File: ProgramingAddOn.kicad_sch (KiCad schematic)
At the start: 25 parts, among them J1 USB_B_Mini, J4 Conn_01x12_Male, J5 Conn_01x12_Female, SW1 SW_DIP_x02, SW2 SW_Push, SW3 SW_Push, SW4 SW_Push, SW5 SW_DIP_x04, SW6 SW_Push, SW7 SW_DIP_x04, U1 CP2102N-Axx-xQFN20

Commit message: Add schematic PDF and PCB rendering
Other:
- company: (none) -> Eric Dynowski
- title: (none) -> SuperCon Badge Programer with USB
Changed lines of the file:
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@@
 (kicad_sch (version 20211123) (generator eeschema)
   (paper "A4")
+  (title_block
+    (title "SuperCon Badge Programer with USB")
+    (date "11/12/22")
+    (rev "v0.1")
+    (company "Eric Dynowski")
+  )
   (junction (at 181.61 67.31) (diameter 0) (color 0 0 0 0)
   )

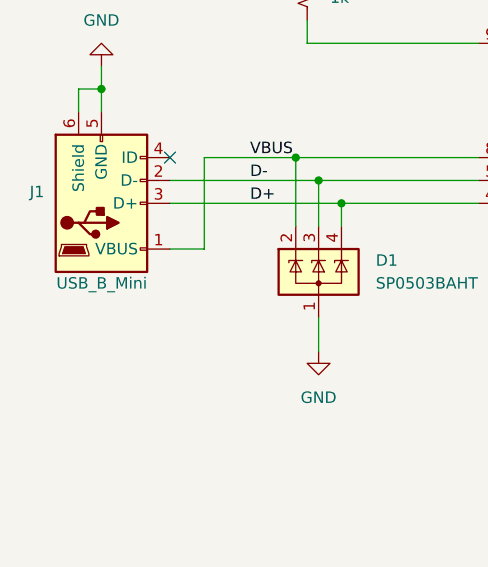
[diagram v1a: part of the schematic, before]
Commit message: Update part descriptions. Change USB mini to micro.
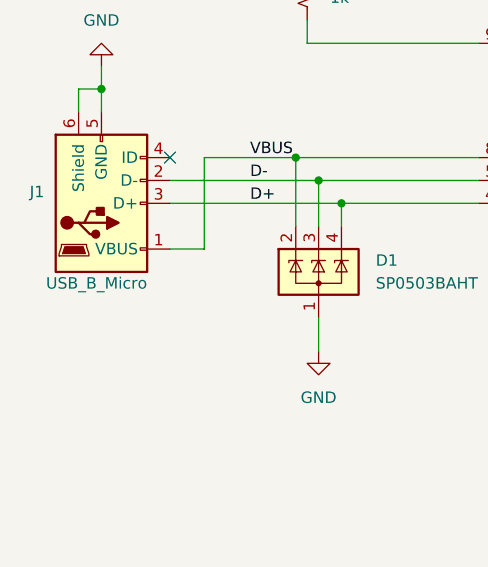
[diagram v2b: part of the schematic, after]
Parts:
- J1: value USB_B_Mini -> USB_B_Micro
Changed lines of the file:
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@@
       (effects (font (size 1.27 1.27)) (justify right))
     )
-    (property "Value" "USB_B_Mini" (id 1) (at 46.99 95.25 0)
+    (property "Value" "USB_B_Micro" (id 1) (at 46.99 95.25 0)
       (effects (font (size 1.27 1.27)) (justify right))
     )
@@
     )
     (path "/b78efc52-662a-4eed-bdbe-033b4b358b00"
-      (reference "J1") (unit 1) (value "USB_B_Mini") (footprint "Connector_USB:USB_Micro-B_Amphenol_10118194_Horizontal")
+      (reference "J1") (unit 1) (value "USB_B_Micro") (footprint "Connector_USB:USB_Micro-B_Amphenol_10118194_Horizontal")
     )
     (path "/0af65d1a-8a8e-409f-ae96-fab30774b7ba"
